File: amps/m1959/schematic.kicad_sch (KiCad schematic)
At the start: 95 parts, among them T1 OT

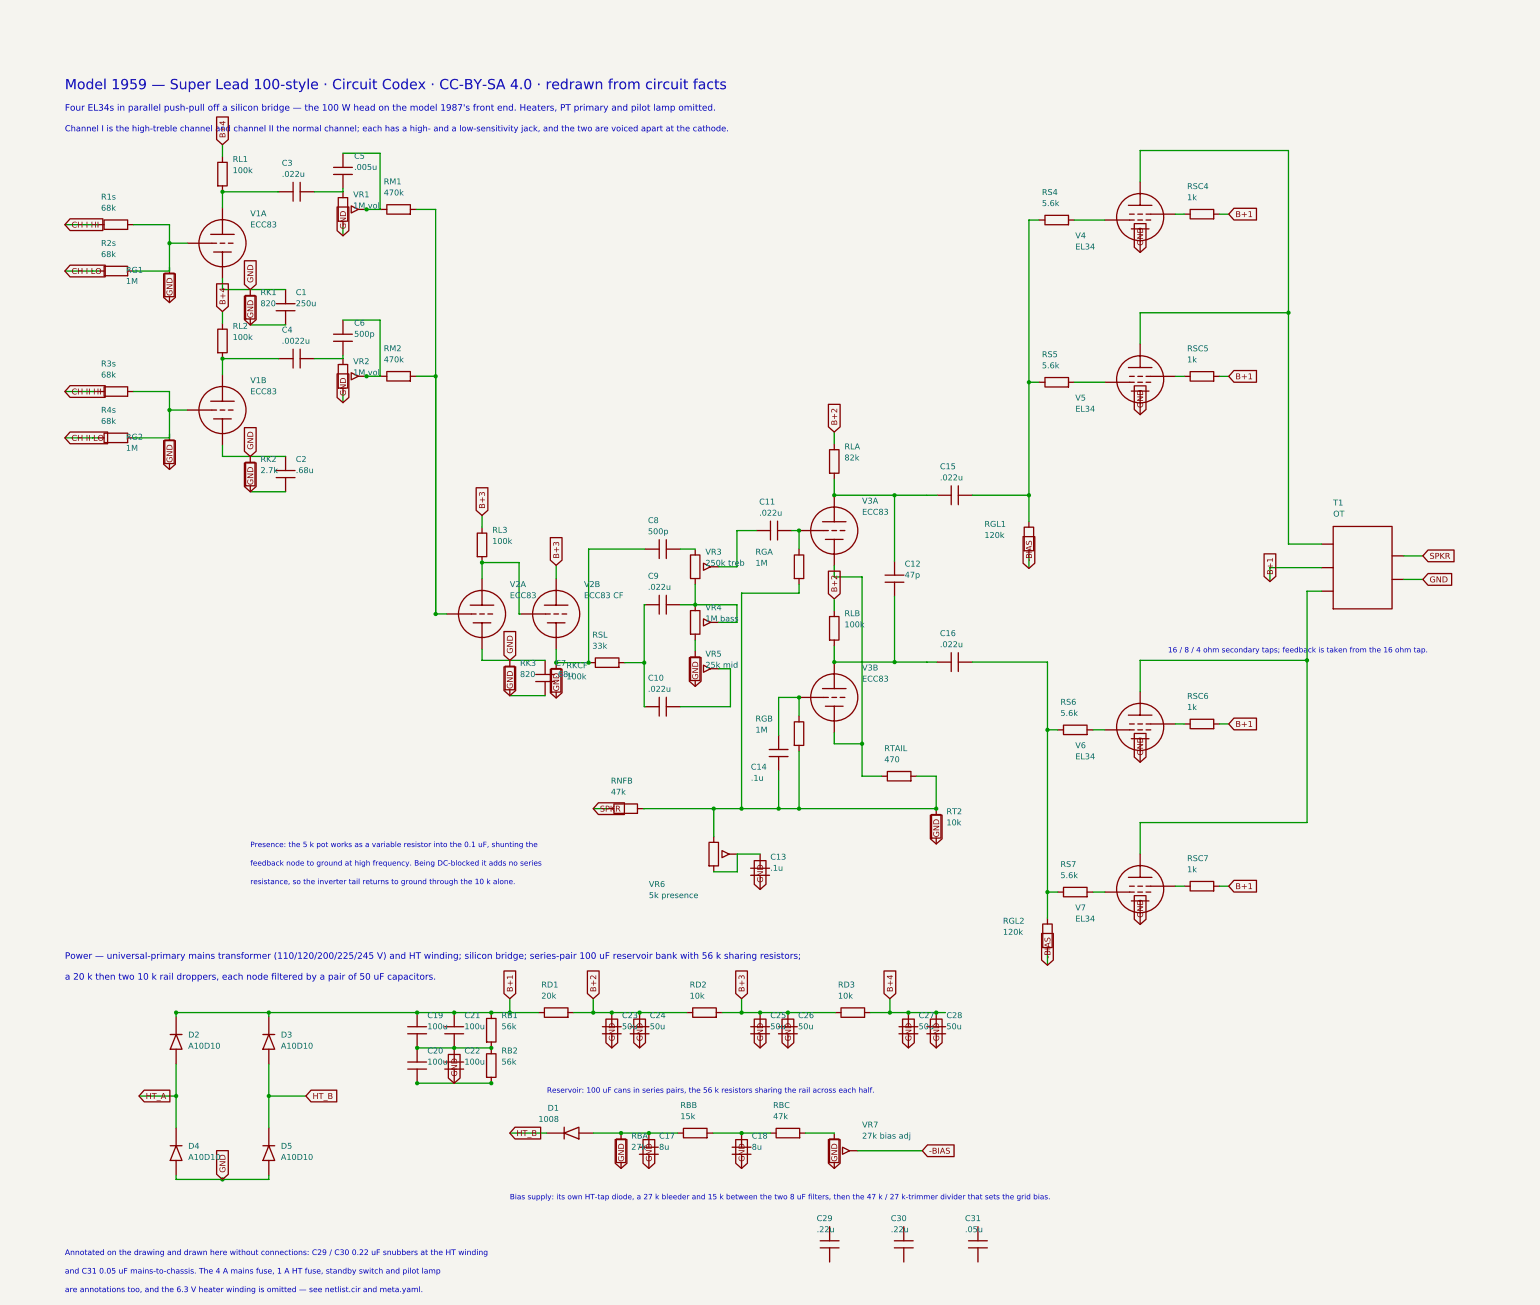
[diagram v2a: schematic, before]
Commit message: Fix: schematic sheets — real title block, fitted paper, no lettering through circuitry
Every sheet in the corpus shipped with an EMPTY title block ("Title:" and
"Date:" blank, default "Sheet /" furniture) laid onto a fixed A4/A3 page
regardless of the drawing's size, with prose annotations placed by hand
wherever a coordinate looked free when the amp was first drawn. The result
read as an unfinished alpha under a `verified` badge: KiCanvas's default view
is `zoom_to_page()`, so a 150 x 110 mm circuit on an A3 sheet opened as a
postage stamp, and later edits had pushed live circuitry under the prose.

schematic_lib.py — the builder now records each element as a (kind, points,
extra) tuple instead of a finished string, so `write()` can measure and move
what it emits:

- emits a real `(title_block …)` read from the amp's own meta.yaml — Title =
  designation + style, Date = the verification (or added) date, Rev = the
  verification status, Company = Circuit Codex, plus the licence and source
  URL as comments. Fixes all 34 sheets from one place;
- emits `(paper "User" w h)` cut to the drawing, translated to a fixed margin,
  with the bottom 34 mm strip reserved for the worksheet's title block. Sheet
  utilisation of the drawable area went from as low as ~20% to 92-98%;
- `note()` queues prose into a wrapped band under the circuit, and `caption()`
  places a section heading over the block it names, nudging it clear if it
  would print through anything;
- per-symbol default label offsets (the old single default printed every pot's
  value through its own wiper arrow and every transformer's designator through
  its body), plus `place_labels()`, which moves any designator/value block that
  would print over ink;
- transformers and chokes are drawn, not boxed: iron core between two windings,
  centre taps where the part has them, and an optional `spec` lettering slot for
  a ratio or impedance;
- `gnd()` takes a direction, because a flag defaulting to "down" at the HEAD of
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
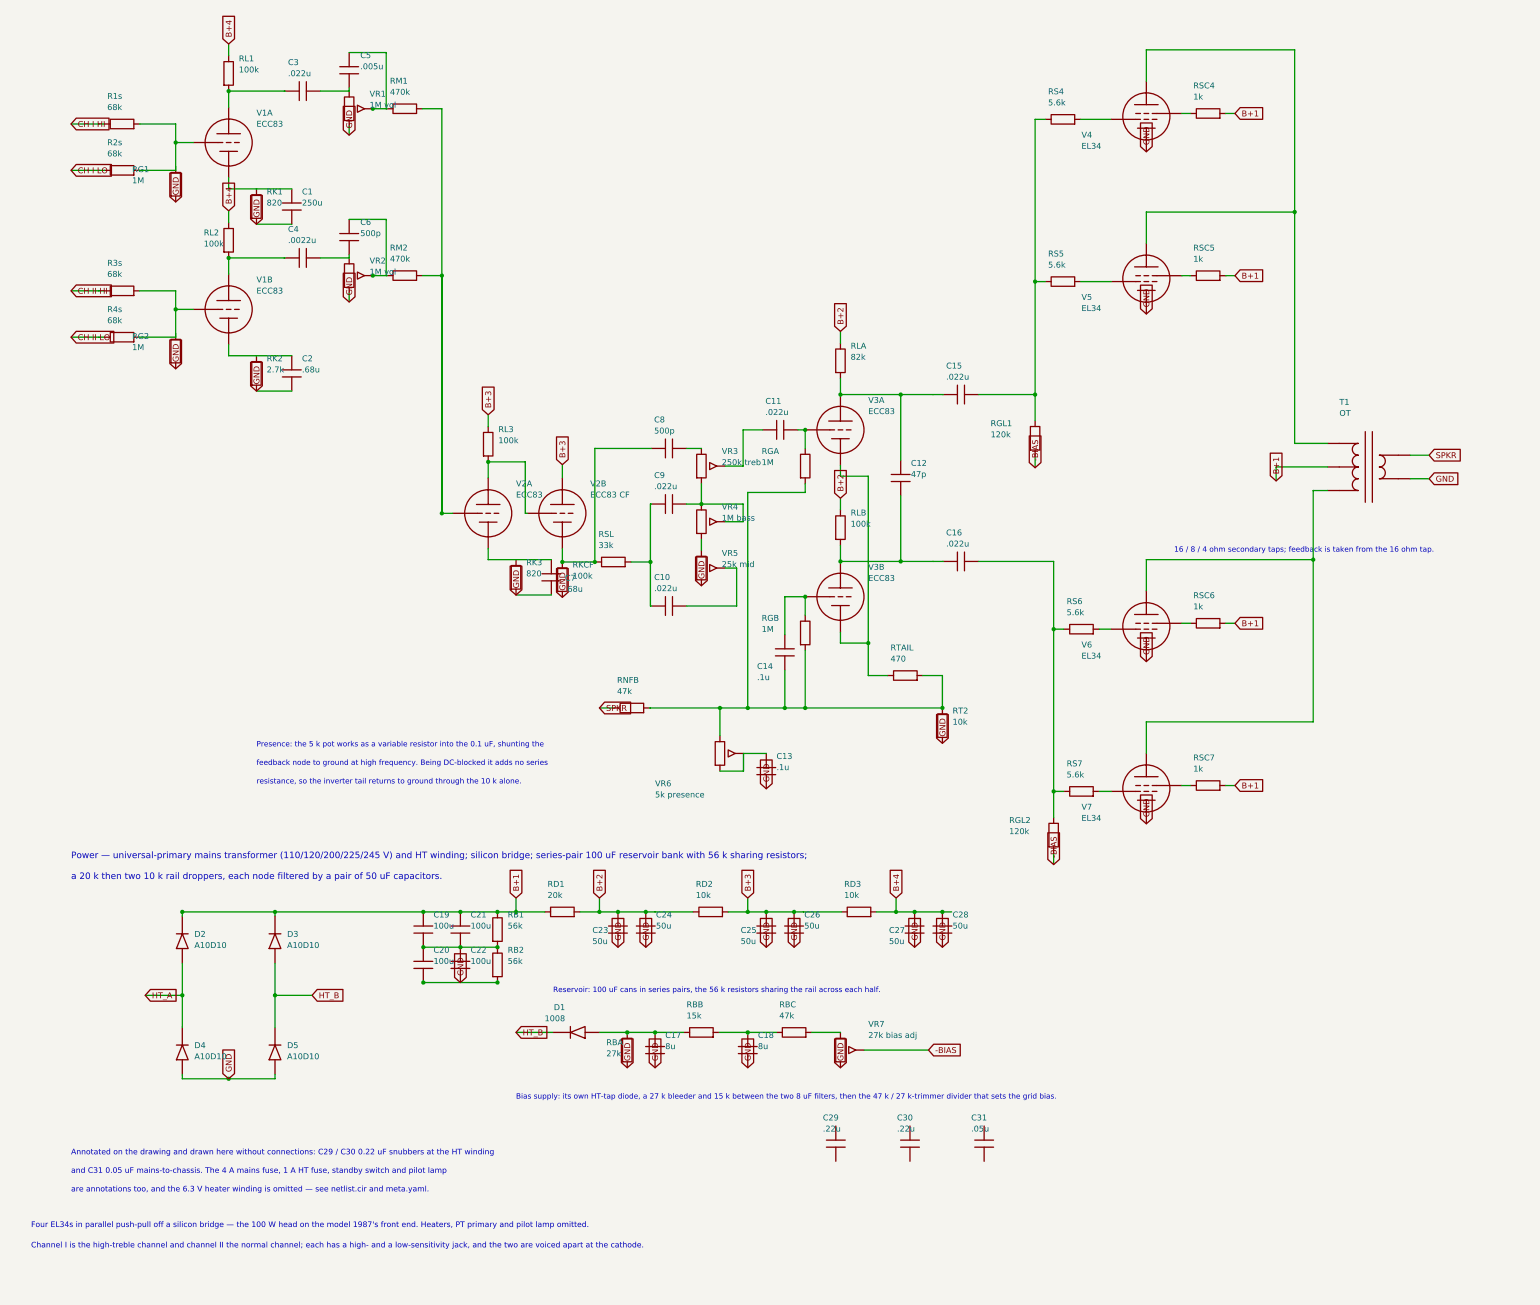
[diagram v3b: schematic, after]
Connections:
- net GND: no longer C1.1, C2.1, C7.1, RK1.1, RK2.1, RK3.1, V1A.3 (K), V1B.3 (K), V2A.3 (K)
- new net: C1.1, RK1.1, V1A.3 (K)
- new net: C2.1, RK2.1, V1B.3 (K)
- new net: C7.1, RK3.1, V2A.3 (K)
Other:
- note removed: "Model 1959 — Super Lead 100-style · Circuit Codex · CC-BY-SA 4.0 · redrawn from circuit facts"
- company: (none) -> Circuit Codex
- title: (none) -> M1959 — Super Lead 100-style

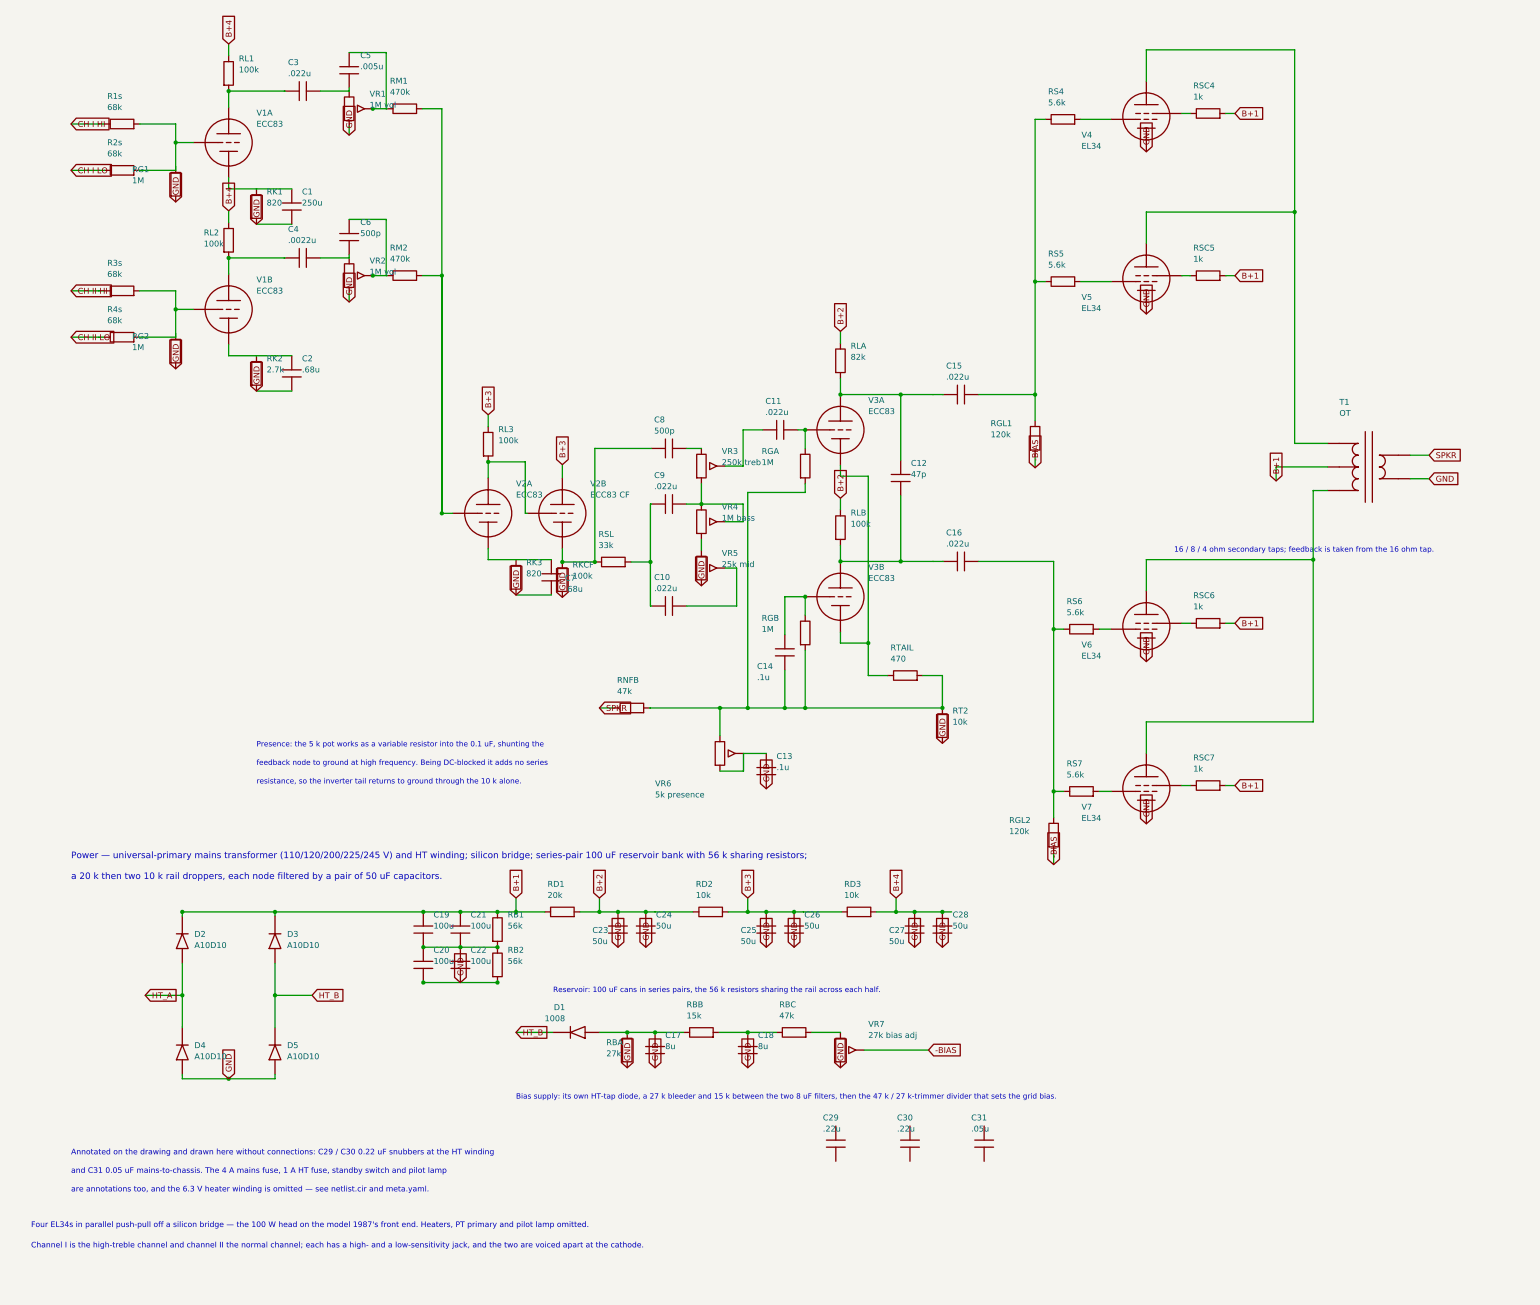
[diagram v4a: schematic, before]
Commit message: Fix: label-wire abutments the gate cannot see, caught by reading pixels
Four sites from the closing visual pass, each a designator or value line
sitting on live wiring below gate sensitivity (wires are not a clash class,
and the old placement ruler under-read text width):

- 5F6-A: RB2's block, squeezed into the 2.5 mm channel beside C15, printed
  through its own resistor body and into C15b's designator. Authored anchor
  now letters it above the supply wire, between RB1's lettering and the -48V
  flag — the one clear pocket in that cramped bias block.
- 6G4: the Speed pot's "4M-RA speed" value line lay on the oscillator ladder
  wire and CTO2's pin; anchored clear (the true-ruler placer settles it left
  of the pot).
- 6G5: RNFB's vertical lettering straddled the NFB wire itself. Drawn
  directly instead of via series_h so the block can be pinned horizontal
  under the part. Also: the tremolo caption was a 175 mm single-sentence
  banner — wider than any clear band on the sheet, printing across the bias
  diodes wherever it was placed. It keeps its headline beside the V3 bottle;
  the mechanism sentence is a note, and notes live in the band.
- 1959: both volume pots' "1M vol" crossed the wiper wire and RM1/RM2's
  pins; anchored clear of the pot body (placer settles them left).

6G6-B's RK2B/CK2B crowding (the fourth verdict item) needed no draw-script
change: the renderer-metric placer from the previous commit already moves the
block clear of the tie wire.

🤖 Generated with [Claude Code](https://claude.com/claude-code)

Co-Authored-By: Claude Fable 5 <noreply@anthropic.com>
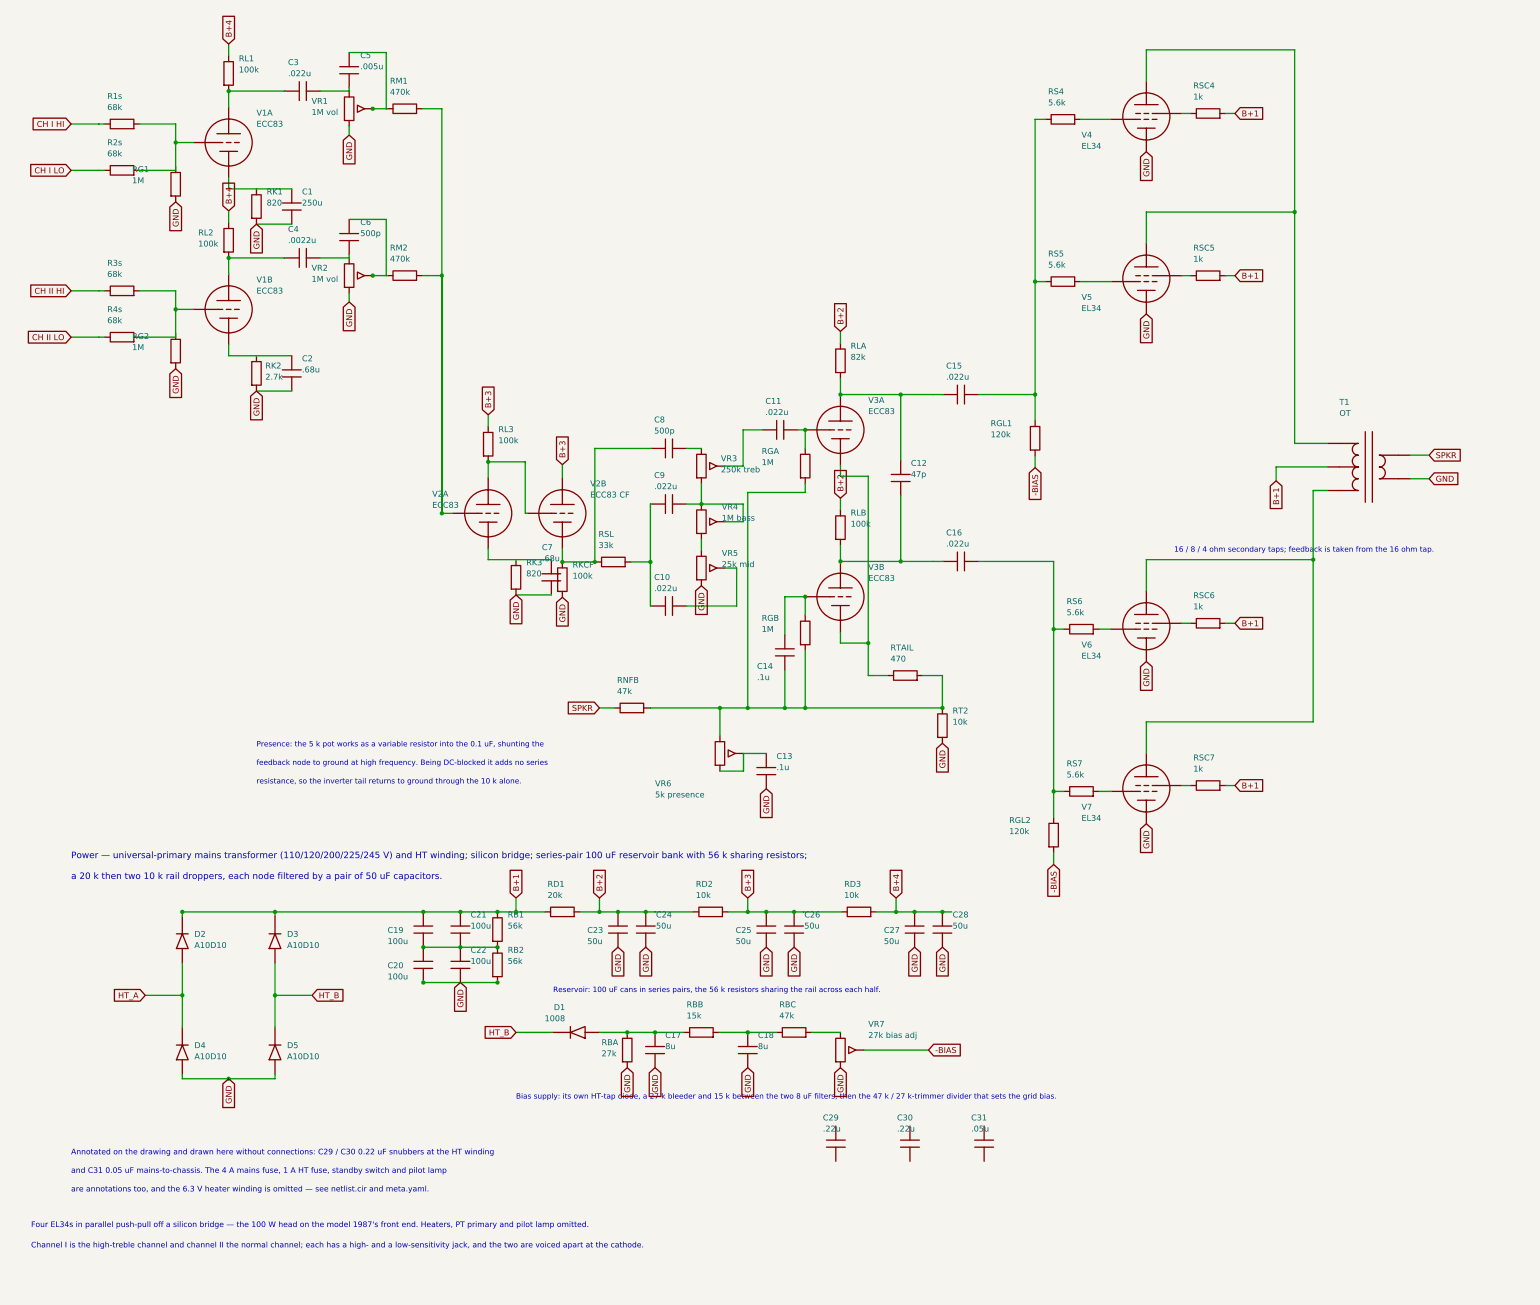
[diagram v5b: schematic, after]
